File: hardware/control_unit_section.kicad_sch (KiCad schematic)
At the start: 2 parts, among them U1 ESP32 S2 Mini

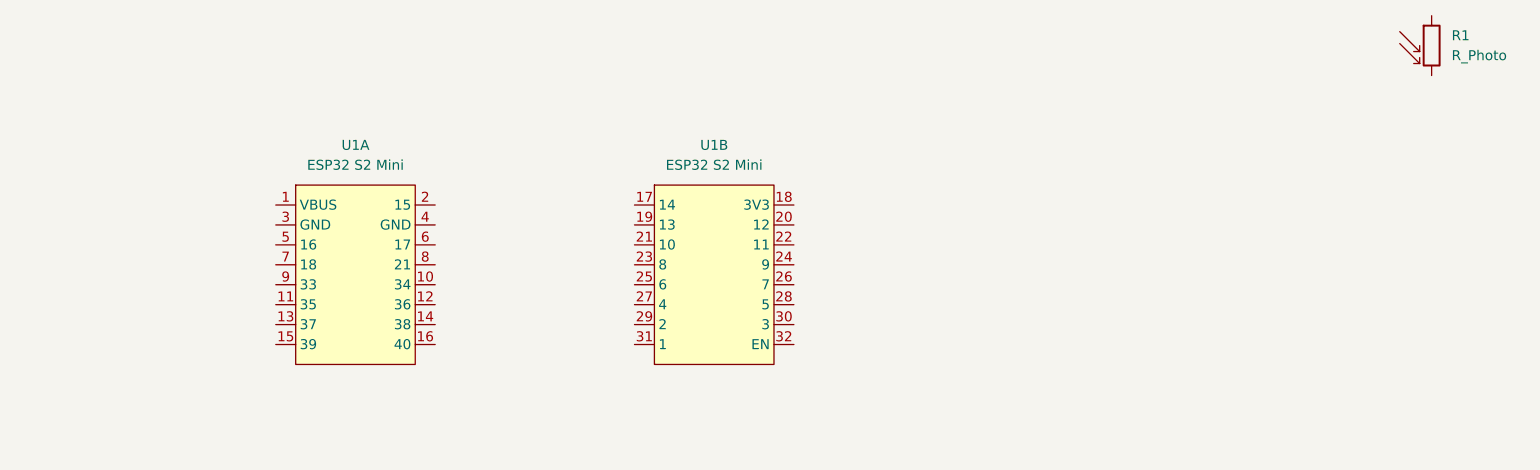
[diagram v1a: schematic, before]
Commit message: Human Interface section finished
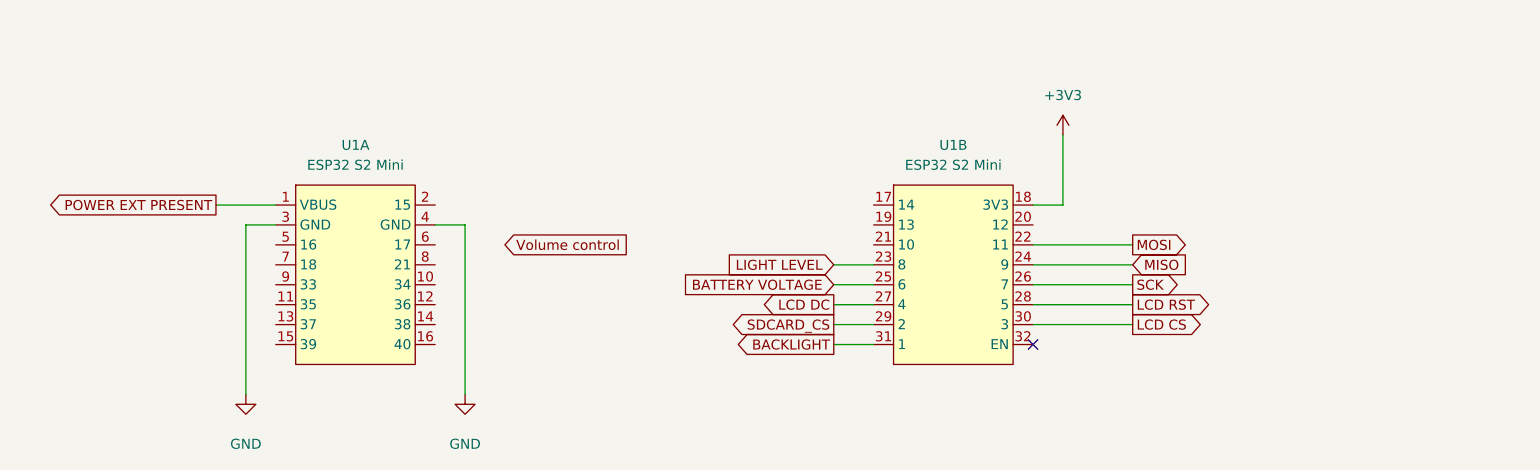
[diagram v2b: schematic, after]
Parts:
- removed R1: R_Photo, symbol Device:R_Photo
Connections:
- net POWER EXT PRESENT: now reaches U1.1 (VBUS)
- net GND: now reaches U1.3 (GND)
- net GND: now also U1.4 (GND)
- net +3V3: now reaches U1.18 (3V3)
- net MOSI: now reaches U1.22 (11)
- net LIGHT LEVEL: now reaches U1.23 (8)
- net MISO: now reaches U1.24 (9)
- net BATTERY VOLTAGE: now reaches U1.25 (6)
- net SCK: now reaches U1.26 (7)
- net LCD DC: now reaches U1.27 (4)
- net LCD RST: now reaches U1.28 (5)
- net SDCARD_CS: now reaches U1.29 (2)
- net LCD CS: now reaches U1.30 (3)
- net BACKLIGHT: now reaches U1.31 (1)
- no-connect marks 0 -> 1
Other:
- moved on the sheet: U1B
